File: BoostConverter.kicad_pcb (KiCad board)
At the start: 2 copper layers, 68.6 x 45.7 mm, 20 parts, among them Q1 Q_NMOS_GDS, U7 Max1771

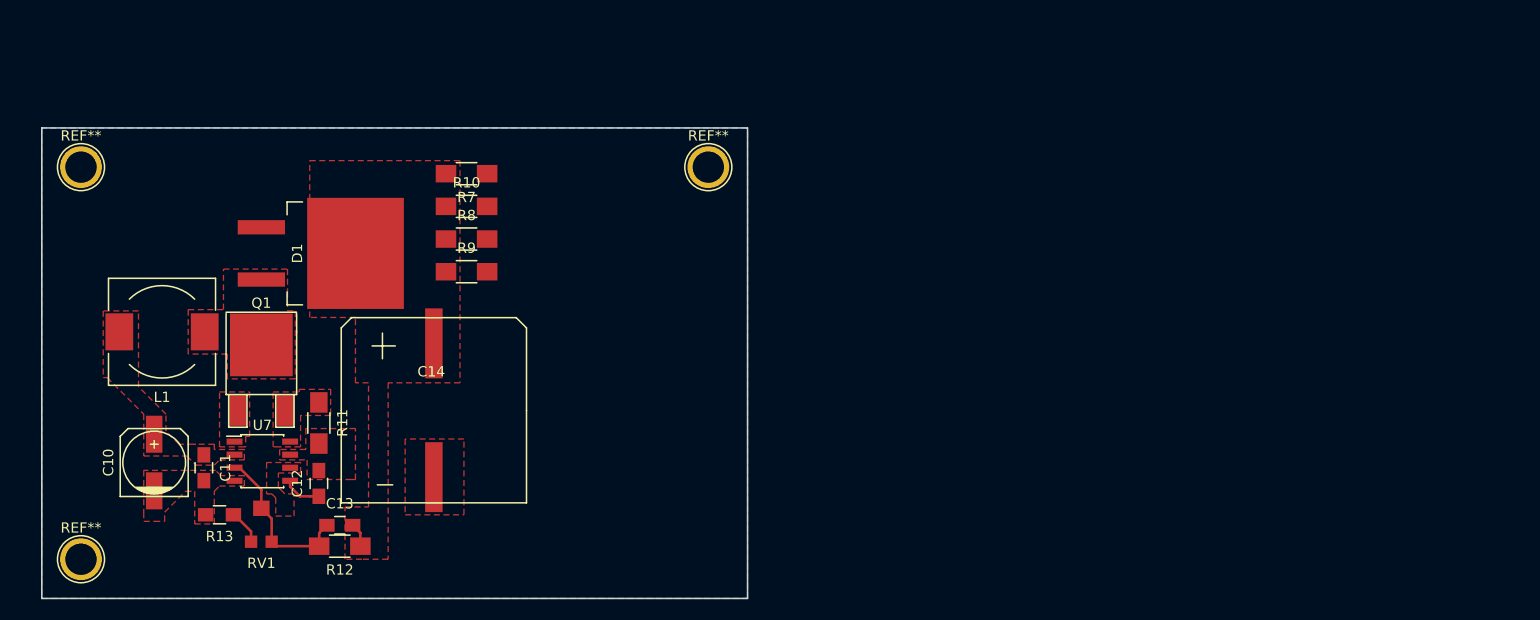
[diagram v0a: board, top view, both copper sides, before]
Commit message: isolated boost converter
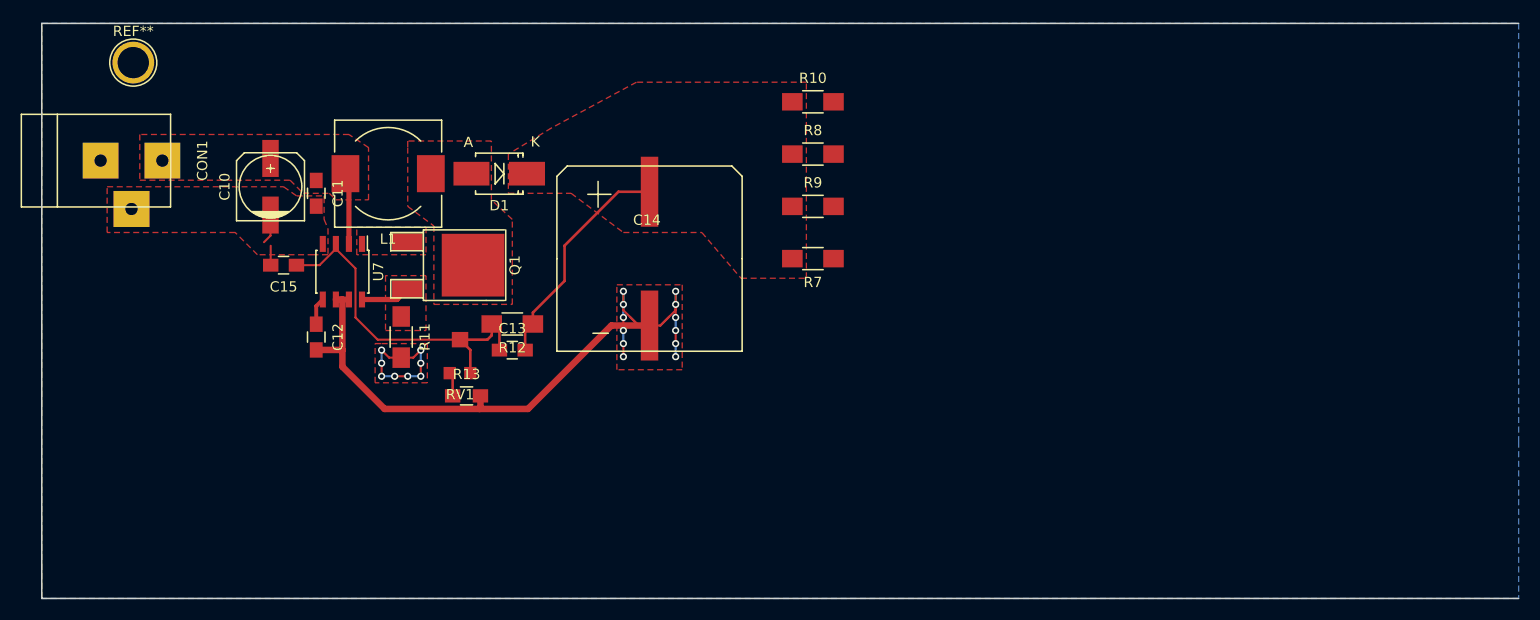
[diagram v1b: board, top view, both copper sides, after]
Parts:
- removed the REF** at (64.8, -41.9)
- removed the REF** at (3.81, -41.9)
- removed the REF** at (3.81, -3.81)
- added C15: 10n, Capacitors_SMD:C_0805_HandSoldering, F.Cu at (23.5, -32.4)
- added CON1: BARREL_JACK, Connect:BARREL_JACK, F.Cu at (5.51, -42.5)
- added REF**: 1pin, Connect:1pin, F.Cu at (8.89, -52.1)
- D1: footprint Footprints:TO-263-ForDiode -> Diodes_SMD:SMB_Handsoldering
- moved R10 35.2 mm to (74.9, -48.3)
- moved R7 34.7 mm to (74.9, -33.0)
- moved R8 34.7 mm to (74.9, -43.2)
- moved R9 34.2 mm to (74.9, -38.1)
- moved C10 29.1 mm to (22.2, -40.0)
- moved C11 28.8 mm to (26.7, -39.4)
- moved R12 27.3 mm to (45.7, -26.7)
- moved L1 26.8 mm to (33.7, -41.3)
- moved R13 26.6 mm to (41.3, -19.7), turned to 0 degrees
- moved C14 25.6 mm to (59.1, -33.0)
- moved RV1 25.3 mm to (40.6, -23.5)
- moved D1 24.4 mm to (44.5, -41.3), turned to 180 degrees
- moved C13 23.9 mm to (45.7, -24.1)
- moved Q1 20.0 mm to (35.6, -32.4), turned to 270 degrees
- moved U7 20.0 mm to (29.2, -31.8), turned to 270 degrees
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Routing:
- net GND: track 0.00 -> 89.7 mm, vias 0 -> 20
- net 170V: track 2.34 -> 22.2 mm
- net Net-(C13-Pad1): track 16.1 -> 34.4 mm
- net +9V: track 0.00 -> 6.97 mm
- net Net-(Q1-Pad3): track 0.00 -> 4.88 mm
- net Net-(C12-Pad1): track 3.74 -> 2.66 mm
- net Net-(R13-Pad1): track 3.38 -> 2.33 mm
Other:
- board size 68.6 x 45.7 mm -> 143.5 x 55.9 mm
- net class Default: clearance 0.2032 -> 0.2; trace_width 0.2032 -> 0.1524; via_dia 0.762 -> 0.7; via_drill 0.3302 -> 0.4
- rule trace_clearance: 0.2032 -> 0.2
- rule trace_min: 0.2 -> 0.1524
